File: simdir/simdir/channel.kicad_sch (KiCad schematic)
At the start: 48 parts, among them Q1 BC847, Q2 BC847, Q3 BC847, Q4 BC847, Q5 BC847, Q6 BC847, Q7 BC847, Q8 BC847, U1 MASWSS0178, U10 MASWSS0178, U11 MASWSS0178, U12 MASWSS0178, U13 MASWSS0178, U14 MASWSS0178, U15 MASWSS0178, U16 MASWSS0178, U2 MASWSS0178, U3 MASWSS0178, U4 MASWSS0178, U5 MASWSS0178, U6 MASWSS0178, U7 MASWSS0178, U8 MASWSS0178, U9 MASWSS0178

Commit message: Update component spacing.
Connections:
- net RF1_meander: now reaches U2.5 (RF2), U6.8 (RF1)
- net RF1_ref: now reaches U2.8 (RF1), U6.5 (RF2)
- net RF5_ref: now reaches U10.8 (RF1), U14.5 (RF2)
- net RF5_meander: now reaches U10.5 (RF2), U14.8 (RF1)
- net RF3_meander: now reaches U4.5 (RF2), U8.8 (RF1)
- net RF2_ref: now reaches U3.8 (RF1), U7.5 (RF2)
- net RF2_meander: now reaches U3.5 (RF2), U7.8 (RF1)
- net RF6_meander: now reaches U11.5 (RF2), U15.8 (RF1)
- net RF6_ref: now reaches U11.8 (RF1), U15.5 (RF2)
- net RF4_ref: now reaches U13.5 (RF2), U9.8 (RF1)
- net RF4_meander: now reaches U13.8 (RF1), U9.5 (RF2)
- net RF7_meander: now reaches U12.5 (RF2), U16.8 (RF1)
- net RF7_ref: now reaches U12.8 (RF1), U16.5 (RF2)
- net RF0_ref: now reaches U1.8 (RF1), U5.5 (RF2)
- net RF0_meander: now reaches U1.5 (RF2), U5.8 (RF1)
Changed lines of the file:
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@@
+		)
+	)
+	(label "RF3_ref"
+		(at 64.77 109.22 0)
+		(effects
+			(font
+				(size 1.27 1.27)
+			)
+			(justify left bottom)
+		)
+	)
+	(label "RF1_ref"
+		(at 66.04 55.88 0)
+		(effects
+			(font
+				(size 1.27 1.27)
+			)
+			(justify left bottom)
+		)
+	)
+	(label "RF2_meander"
+		(at 67.31 91.44 0)
+		(effects
+			(font
+				(size 1.27 1.27)
+			)
+			(justify left bottom)
+		)
+	)
+	(label "RF7_meander"
+		(at 194.31 118.11 0)
+		(effects
+			(font
+				(size 1.27 1.27)
+			)
+			(justify left bottom)
+		)
+	)
+	(label "RF5_ref"
+		(at 191.77 55.88 0)
+		(effects
+			(font
+				(size 1.27 1.27)
+			)
+			(justify left bottom)
+		)
+	)
+	(label "RF4_meander"
+		(at 193.04 36.83 0)
+		(effects
+			(font
+				(size 1.27 1.27)
+			)
+			(justify left bottom)
+		)
+	)
+	(label "RF7_ref"
+		(at 193.04 110.49 0)
+		(effects
+			(font
+				(size 1.27 1.27)
+			)
+			(justify left bottom)
+		)
+	)
+	(label "RF0_meander"
+		(at 67.31 36.83 0)
+		(effects
+			(font
+				(size 1.27 1.27)
+			)
+			(justify left bottom)
+		)
+	)
+	(label "RF0_ref"
+		(at 67.31 29.21 0)
+		(effects
+			(font
+				(size 1.27 1.27)
+			)
+			(justify left bottom)
+		)
+	)
+	(label "RF2_ref"
+		(at 66.04 83.82 0)
+		(effects
+			(font
+				(size 1.27 1.27)
+			)
+			(justify left bottom)
+		)
+	)
+	(label "RF6_ref"
+		(at 191.77 83.82 0)
+		(effects
+			(font
+				(size 1.27 1.27)
+			)
+			(justify left bottom)
+		)
+	)
+	(label "RF1_meander"
+		(at 68.58 63.5 0)
+		(effects
+			(font
+				(size 1.27 1.27)
+			)
+			(justify left bottom)
+		)
+	)
+	(label "RF4_ref"
+		(at 191.77 29.21 0)
+		(effects
+			(font
+				(size 1.27 1.27)
+			)
+			(justify left bottom)
+		)
+	)
+	(label "RF3_meander"
+		(at 67.31 118.11 0)
+		(effects
+			(font
+				(size 1.27 1.27)
+			)
+			(justify left bottom)
+		)
+	)
+	(label "RF6_meander"
+		(at 193.04 91.44 0)
+		(effects
+			(font
+				(size 1.27 1.27)
+			)
+			(justify left bottom)
+		)
+	)
+	(label "RF5_meander"
+		(at 193.04 63.5 0)
+		(effects
+			(font
+				(size 1.27 1.27)
+			)
+			(justify left bottom)
 		)
 	)

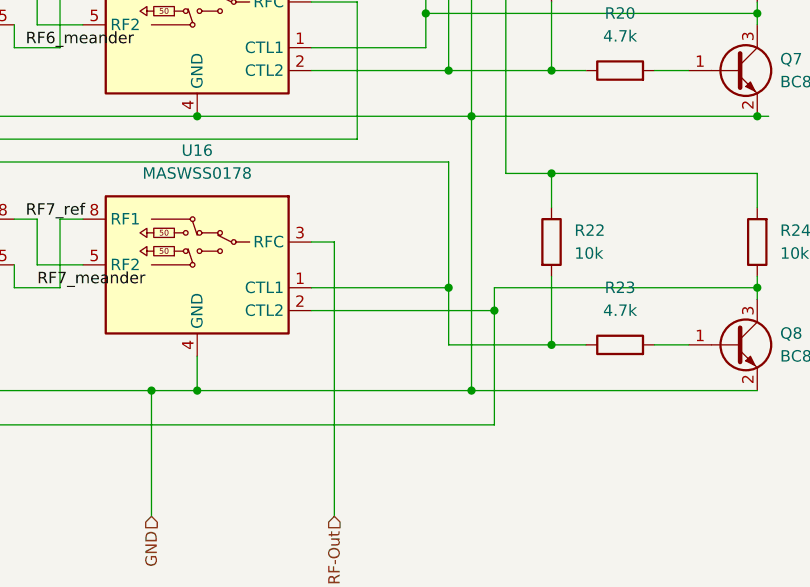
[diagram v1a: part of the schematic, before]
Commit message: Routed control logic for switches.
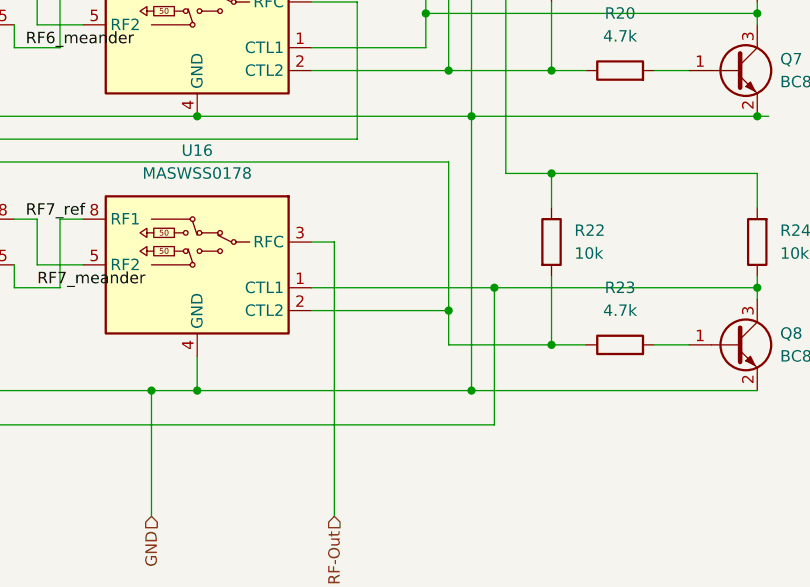
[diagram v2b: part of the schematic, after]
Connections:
- net at Q8.3 (C), R24.1, U12.2 (CTL2): now also U16.1 (CTL1); no longer U16.2 (CTL2)
- net at R22.2, R23.1, U12.1 (CTL1): now also U16.2 (CTL2); no longer U16.1 (CTL1)
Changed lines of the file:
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@@
 	)
 	(junction
-		(at 116.84 93.98)
+		(at 245.11 118.11)
 		(diameter 0)
 		(color 0 0 0 0)
 	)
 	(junction
-		(at 212.09 129.54)
+		(at 116.84 93.98)
 		(diameter 0)
 		(color 0 0 0 0)
 	)
 	(junction
-		(at 251.46 124.46)
+		(at 212.09 129.54)
 		(diameter 0)
 		(color 0 0 0 0)
 	)
 	(junction
-		(at 240.03 118.11)
+		(at 251.46 124.46)
 		(diameter 0)
 		(color 0 0 0 0)
@@
 	)
 	(junction
-		(at 251.46 105.41)
+		(at 240.03 120.65)
 		(diameter 0)
 		(color 0 0 0 0)
 	)
 	(junction
-		(at 245.11 120.65)
+		(at 251.46 105.41)
 		(diameter 0)
 		(color 0 0 0 0)
@@
 	(wire
 		(pts
-			(xy 240.03 118.11) (xy 240.03 124.46)
+			(xy 240.03 104.14) (xy 240.03 120.65)
 		)
 		(stroke
@@
 	(wire
 		(pts
-			(xy 245.11 120.65) (xy 245.11 133.35)
+			(xy 245.11 118.11) (xy 245.11 133.35)
 		)
 		(stroke
@@
 	(wire
 		(pts
-			(xy 245.11 118.11) (xy 245.11 120.65)
-		)
-		(stroke
-			(width 0)
-			(type default)
-		)
-	)
-	(wire
-		(pts
 			(xy 224.79 36.83) (xy 234.95 36.83)
 		)
@@
 	(wire
 		(pts
-			(xy 66.04 118.11) (xy 71.12 118.11)
+			(xy 224.79 118.11) (xy 245.11 118.11)
 		)
 		(stroke
@@
 	(wire
 		(pts
-			(xy 240.03 104.14) (xy 240.03 118.11)
+			(xy 66.04 118.11) (xy 71.12 118.11)
 		)
 		(stroke
@@
 	(wire
 		(pts
-			(xy 224.79 120.65) (xy 245.11 120.65)
-		)
-		(stroke
-			(width 0)
-			(type default)
-		)
-	)
-	(wire
-		(pts
 			(xy 275.59 16.51) (xy 274.32 16.51)
 		)
@@
 	(wire
 		(pts
+			(xy 224.79 120.65) (xy 240.03 120.65)
+		)
+		(stroke
+			(width 0)
+			(type default)
+		)
+	)
+	(wire
+		(pts
 			(xy 227.33 113.03) (xy 224.79 113.03)
 		)
@@
 	(wire
 		(pts
-			(xy 224.79 118.11) (xy 240.03 118.11)
-		)
-		(stroke
-			(width 0)
-			(type default)
-		)
-	)
-	(wire
-		(pts
 			(xy 34.29 133.35) (xy 34.29 120.65)
 		)
@@
 		)
 		(stroke
+			(width 0)
+			(type default)
+		)
+	)
+	(wire
+		(pts
+			(xy 240.03 120.65) (xy 240.03 124.46)
+		)
+		(stroke

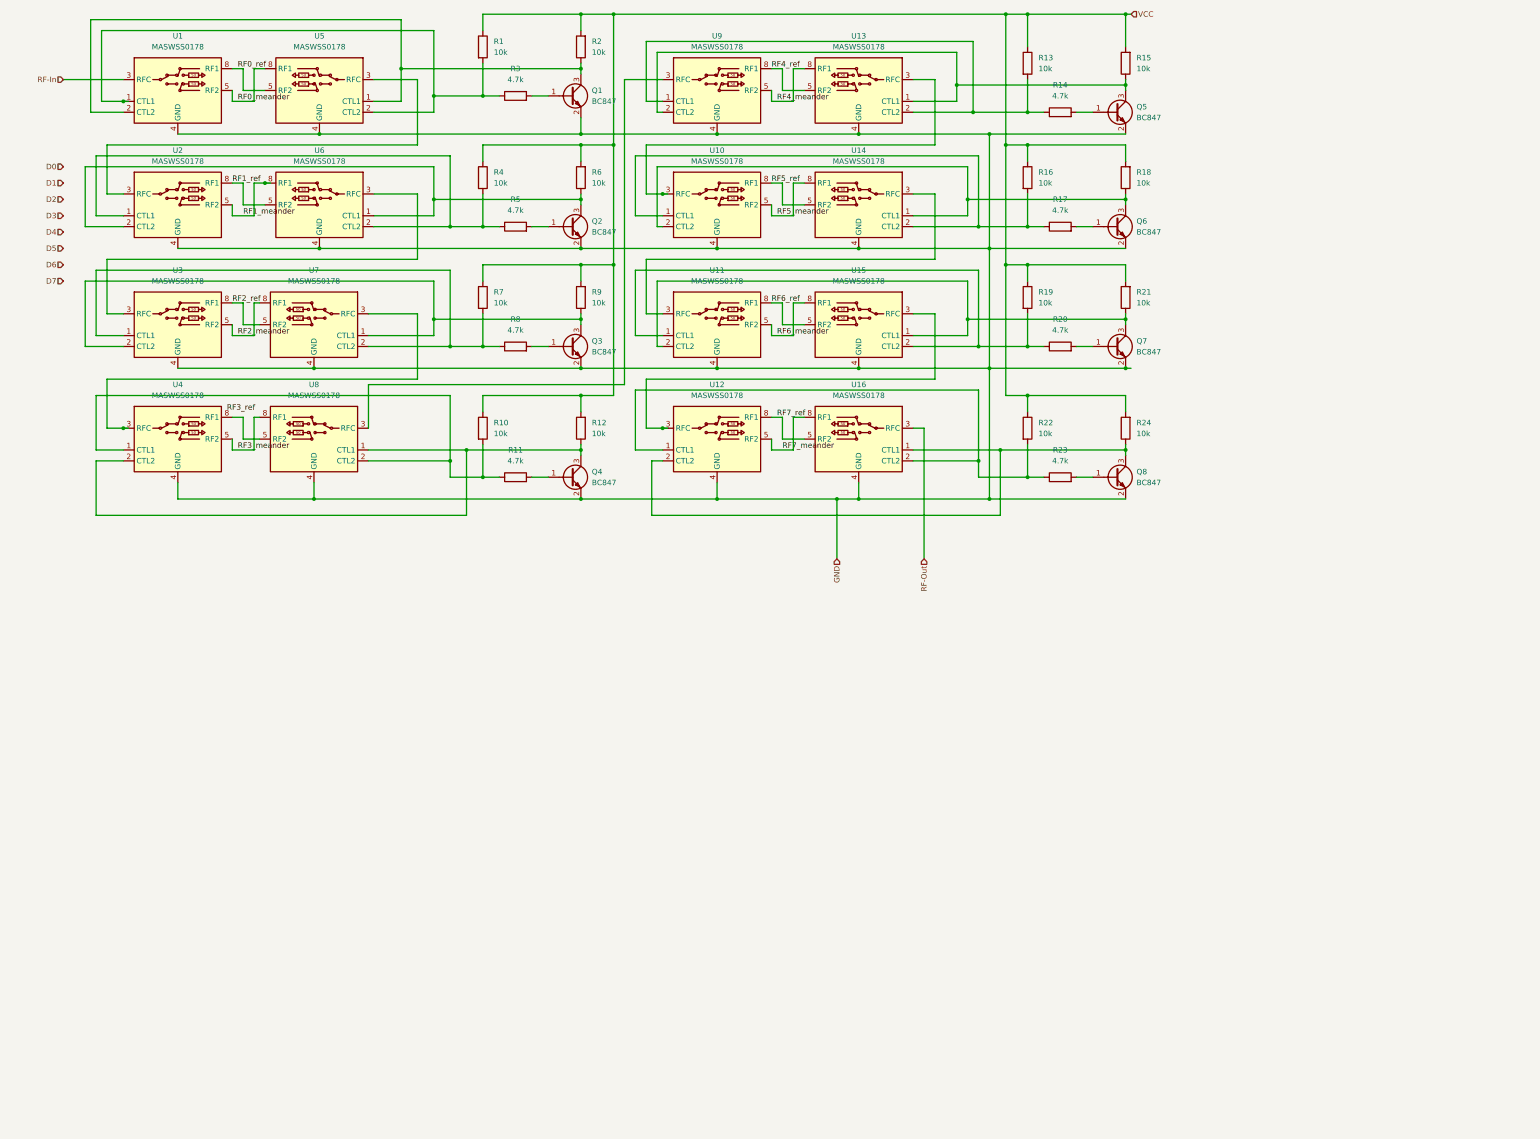
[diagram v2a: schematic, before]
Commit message: Add digital logic to channel
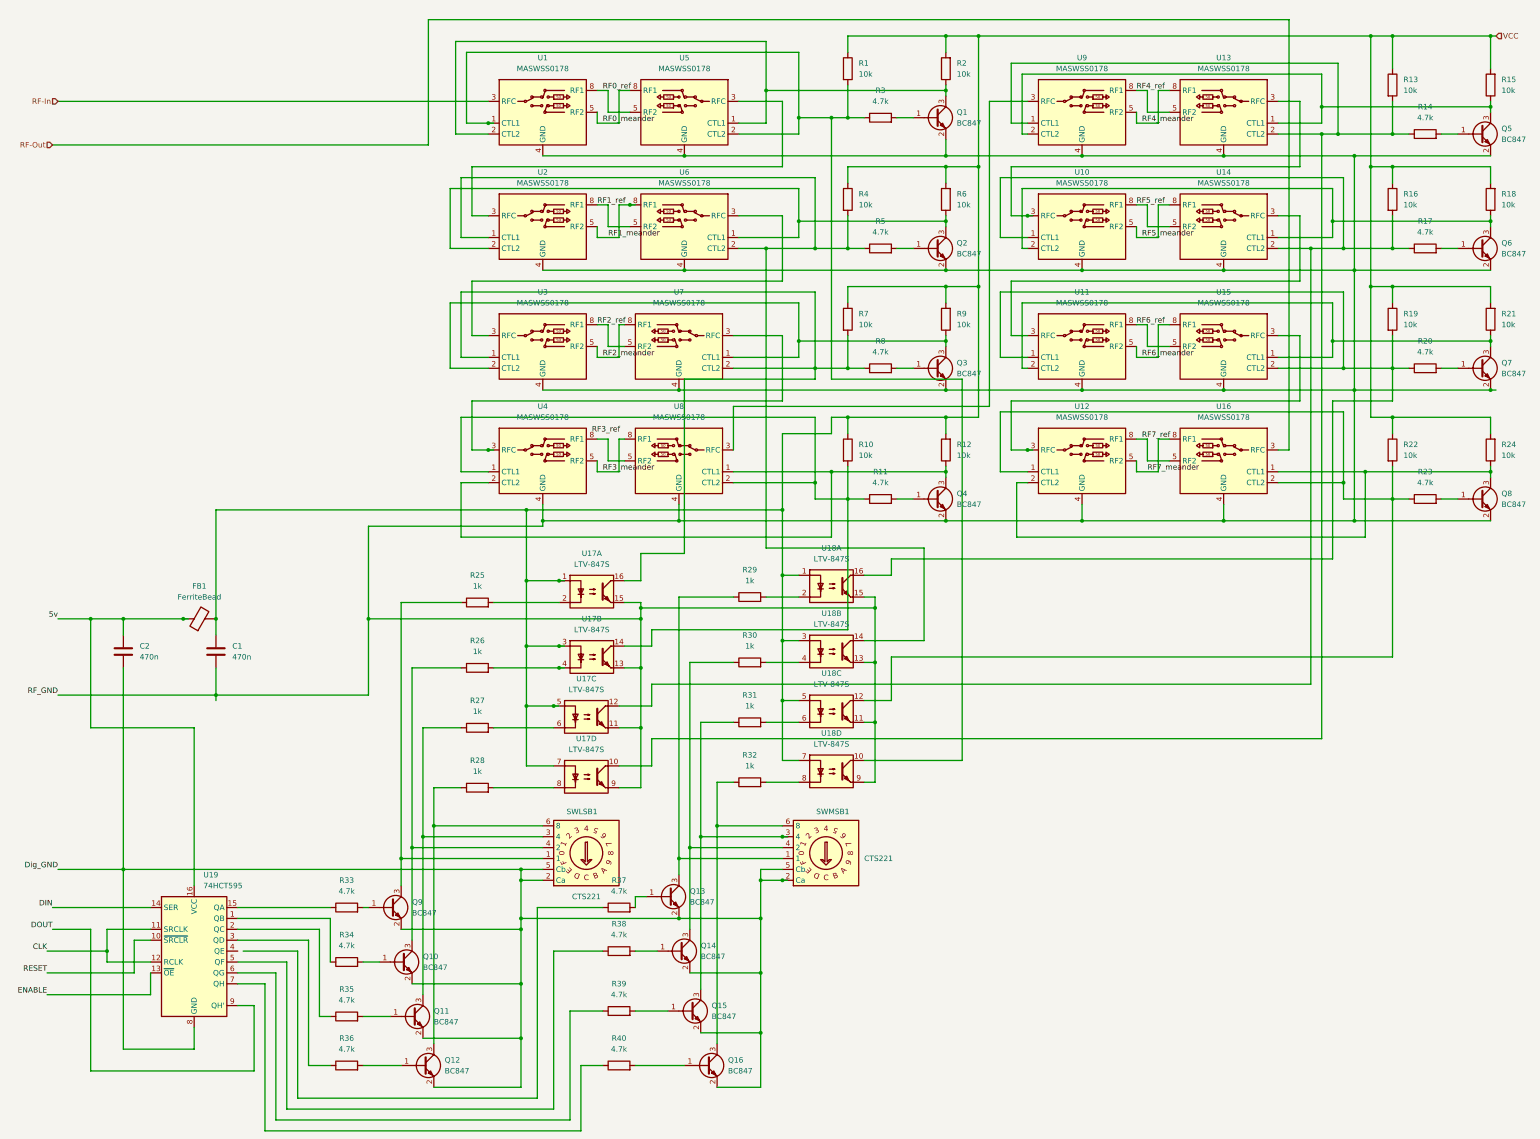
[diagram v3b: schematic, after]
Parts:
- added C1, C2: 470n, Capacitor_SMD:C_0805_2012Metric_Pad1.18x1.45mm_HandSolder, symbol Device:C
- added FB1: FerriteBead, Inductor_SMD:L_0805_2012Metric_Pad1.05x1.20mm_HandSolder, symbol Device:FerriteBead
- added Q10, Q11, Q12, Q13, Q14, Q15, Q16, Q9: BC847, Package_TO_SOT_SMD:SOT-23, symbol Transistor_BJT:BC847
- added R25, R26, R27, R28, R29, R30, R31, R32: 1k, Resistor_SMD:R_0805_2012Metric_Pad1.20x1.40mm_HandSolder, symbol Device:R
- added R33, R34, R35, R36, R37, R38, R39, R40: 4.7k, Resistor_SMD:R_0805_2012Metric_Pad1.20x1.40mm_HandSolder, symbol Device:R
- added SWLSB1, SWMSB1: CTS221, hand:CTS221, symbol hand:CTS221
- added U17, U18: LTV-847S, Package_DIP:SMDIP-16_W9.53mm, symbol Isolator:LTV-847S
- added U19: 74HCT595, Package_SO:SOIC-16_3.9x9.9mm_P1.27mm, symbol 74xx:74HCT595
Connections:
- net VCC: now also C1.1, FB1.2, U17.1, U17.3, U17.5, U17.7, U18.1, U18.3, U18.5, U18.7
- net at R1.2, R3.1, U1.1 (CTL1)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: now also U18.10
- net at R22.2, R23.1, U12.1 (CTL1)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: now also U18.12
- net at R4.2, R5.1, U2.1 (CTL1)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: now also U18.14
- net at R16.2, R17.1, U10.1 (CTL1)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: now also U17.12
- net at R10.2, R11.1, U4.1 (CTL1)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: now also U17.14
- net at R19.2, R20.1, U11.1 (CTL1)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: now also U18.16
- net at R7.2, R8.1, U3.1 (CTL1)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: now also U17.16
- net at R13.2, R14.1, U13.2 (CTL2)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: now also U17.10
- net GND renamed RF_GND
- net RF_GND: now also C1.2, U17.11, U17.13, U17.15, U17.9, U18.11, U18.13, U18.15, U18.9
- new net: Q10.3 (C), R26.1, SWLSB1.4 (2)
- new net: R26.2, U17.4
- new net: Q9.3 (C), R25.1, SWLSB1.1
- new net: R25.2, U17.2
- new net: R33.1, U19.15 (QA)
- new net: Q9.1 (B), R33.2
- new net: R31.2, U18.6
- new net: R38.1, U19.5 (QF)
- new net: Q14.1 (B), R38.2
- new net: R34.1, U19.1 (QB)
- new net: Q10.1 (B), R34.2
- new net: Q14.3 (C), R30.1, SWMSB1.4 (2)
- new net: R30.2, U18.4
- new net: Q11.3 (C), R27.1, SWLSB1.3 (4)
- new net: R27.2, U17.6
- new net: Q12.3 (C), R28.1, SWLSB1.6 (8)
- new net: R28.2, U17.8
- new net: R35.1, U19.2 (QC)
- new net: R36.1, U19.3 (QD)
- new net: R39.1, U19.6 (QG)
- new net: R40.1, U19.7 (QH)
- new net: Q16.1 (B), R40.2
- new net: Q16.3 (C), R32.1, SWMSB1.6 (8)
- new net: Q11.1 (B), R35.2
- new net: Q12.1 (B), R36.2
- new net: Q13.1 (B), R37.2
- new net: Q15.3 (C), R31.1, SWMSB1.3 (4)
- new net: Q15.1 (B), R39.2
- new net: R32.2, U18.8
- new net: Q13.3 (C), R29.1, SWMSB1.1
- new net: R29.2, U18.2
- new net 5v: C2.1, FB1.1, U19.16 (VCC)
- new net CLK: U19.11 (SRCLK), U19.12 (RCLK)
- new net DIN: U19.14 (SER)
- new net DOUT: U19.9 (QH')
- new net Dig_GND: C2.2, Q10.2 (E), Q11.2 (E), Q12.2 (E), Q13.2 (E), Q14.2 (E), Q15.2 (E), Q16.2 (E), Q9.2 (E), SWLSB1.2 (Ca), SWLSB1.5 (Cb), SWMSB1.2 (Ca), SWMSB1.5 (Cb), U19.8 (GND)
- new net ENABLE: U19.13 (~{OE})
- new net RESET: U19.10 (~{SRCLR})
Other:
- moved on the sheet: Q1, Q2, Q3, Q4, Q5, Q6, Q7, Q8, R1, R10, R11, R12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
